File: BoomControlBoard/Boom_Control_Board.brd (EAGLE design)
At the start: 82.5 x 50.8 mm, 43 parts, among them J1 Servo Header, J2 FTDI Header, J7 455-1750-1-ND, U1 ATMEGA328P_TQFP, U2 3.3V/150mA, Y1 16MHz

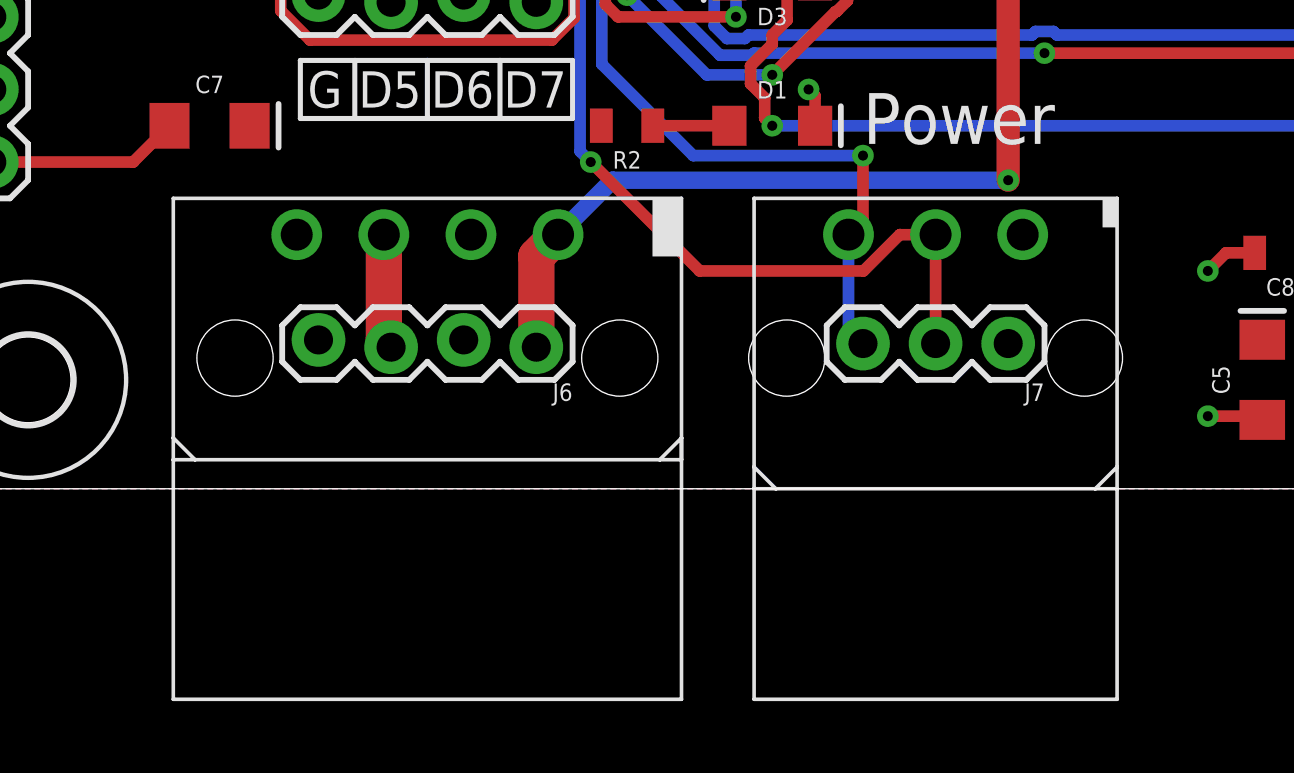
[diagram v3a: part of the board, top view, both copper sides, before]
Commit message: Improved Molex connector footprints.
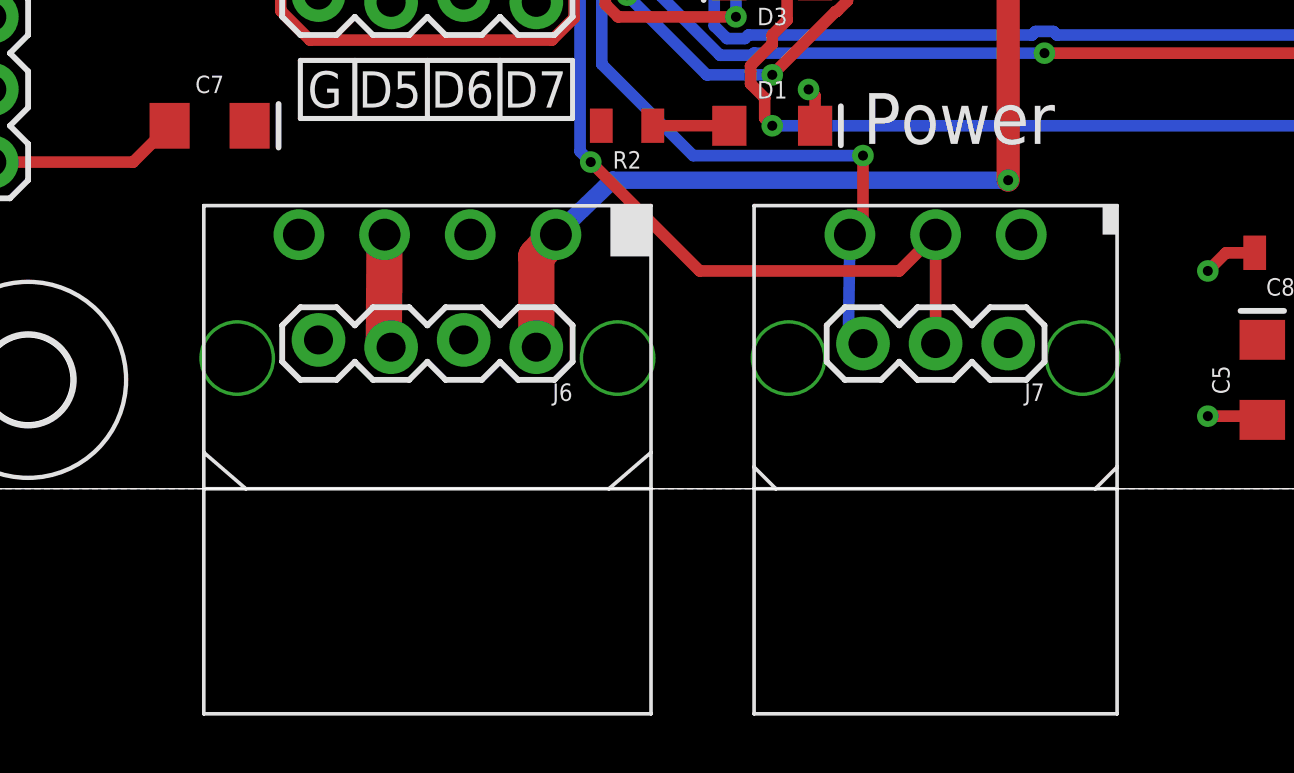
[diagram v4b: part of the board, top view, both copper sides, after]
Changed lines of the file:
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@@
 <attribute name="VALUE" x="24.765" y="13.589" size="0.6096" layer="27" font="vector" ratio="20" rot="R180" align="top-center"/>
 </element>
-<element name="H1" library="holes" library_urn="urn:adsk.eagle:library:237" package="3,0" package3d_urn="urn:adsk.eagle:package:14277/1" value="MOUNT-HOLE3.0" x="3.81" y="3.81" smashed="yes"/>
-<element name="H2" library="holes" library_urn="urn:adsk.eagle:library:237" package="3,0" package3d_urn="urn:adsk.eagle:package:14277/1" value="MOUNT-HOLE3.0" x="78.74" y="3.81" smashed="yes"/>
-<element name="H3" library="holes" library_urn="urn:adsk.eagle:library:237" package="3,0" package3d_urn="urn:adsk.eagle:package:14277/1" value="MOUNT-HOLE3.0" x="3.81" y="46.99" smashed="yes"/>
-<element name="H4" library="holes" library_urn="urn:adsk.eagle:library:237" package="3,0" package3d_urn="urn:adsk.eagle:package:14277/1" value="MOUNT-HOLE3.0" x="78.74" y="46.99" smashed="yes"/>
+<element name="H1" library="holes" library_urn="urn:adsk.eagle:library:237" package="3,0" package3d_urn="urn:adsk.eagle:package:14277/1" value="MOUNT-HOLE3.0" x="3.81" y="3.81" smashed="yes">
+<attribute name="POPULARITY" value="3" x="3.81" y="3.81" size="1.778" layer="27" display="off"/>
+</element>
+<element name="H2" library="holes" library_urn="urn:adsk.eagle:library:237" package="3,0" package3d_urn="urn:adsk.eagle:package:14277/1" value="MOUNT-HOLE3.0" x="78.74" y="3.81" smashed="yes">
+<attribute name="POPULARITY" value="3" x="78.74" y="3.81" size="1.778" layer="27" display="off"/>
+</element>
+<element name="H3" library="holes" library_urn="urn:adsk.eagle:library:237" package="3,0" package3d_urn="urn:adsk.eagle:package:14277/1" value="MOUNT-HOLE3.0" x="3.81" y="46.99" smashed="yes">
+<attribute name="POPULARITY" value="3" x="3.81" y="46.99" size="1.778" layer="27" display="off"/>
+</element>
+<element name="H4" library="holes" library_urn="urn:adsk.eagle:library:237" package="3,0" package3d_urn="urn:adsk.eagle:package:14277/1" value="MOUNT-HOLE3.0" x="78.74" y="46.99" smashed="yes">
+<attribute name="POPULARITY" value="3" x="78.74" y="46.99" size="1.778" layer="27" display="off"/>
+</element>
 <element name="S1" library="SparkFun-Switches" package="TACTILE_SWITCH_SMD_5.2MM" value="RESET" x="28.575" y="34.925" smashed="yes">
 <attribute name="NAME" x="28.575" y="37.592" size="0.6096" layer="25" font="vector" ratio="20" align="bottom-center"/>
@@
 <signal name="12V">
 <contactref element="U$1" pad="PIN1"/>
-<wire x1="24.257" y1="10.795" x2="22.352" y2="8.89" width="0.6096" layer="16"/>
+<wire x1="24.257" y1="10.795" x2="22.2758" y2="8.89" width="0.6096" layer="16"/>
 <wire x1="38.1" y1="10.795" x2="24.257" y2="10.795" width="0.6096" layer="16"/>
 <contactref element="U$4" pad="6"/>
@@
 <wire x1="39.0624" y1="30.47078125" x2="39.0624" y2="26.90635625" width="0.8128" layer="1"/>
 <contactref element="J6" pad="1"/>
-<wire x1="22.352" y1="8.89" x2="21.59" y2="8.128" width="1.27" layer="1"/>
+<wire x1="22.2758" y1="8.89" x2="21.59" y2="8.128" width="1.27" layer="1"/>
 <wire x1="21.59" y1="8.128" x2="21.59" y2="4.953" width="1.27" layer="1"/>
 </signal>
@@
 <contactref element="U$1" pad="PIN3"/>
 <contactref element="J6" pad="3"/>
-<wire x1="16.256" y1="8.89" x2="16.256" y2="5.207" width="1.27" layer="1"/>
+<wire x1="16.2814" y1="8.89" x2="16.256" y2="5.207" width="1.27" layer="1"/>
 <wire x1="16.256" y1="5.207" x2="16.51" y2="4.953" width="1.27" layer="1"/>
 </signal>
@@
 <via x="33.02" y="11.6558" extent="1-16" drill="0.35"/>
 <wire x1="33.02" y1="11.6558" x2="33.02" y2="9.398" width="0.4064" layer="1"/>
-<wire x1="33.02" y1="9.398" x2="32.512" y2="8.89" width="0.4064" layer="1"/>
+<wire x1="33.02" y1="9.398" x2="32.5628" y2="8.89" width="0.4064" layer="1"/>
 <wire x1="23.8816" y1="23.495" x2="23.8816" y2="14.8534" width="0.4064" layer="16"/>
 <wire x1="23.8816" y1="14.8534" x2="27.0792" y2="11.6558" width="0.4064" layer="16"/>
 <wire x1="27.0792" y1="11.6558" x2="33.02" y2="11.6558" width="0.4064" layer="16"/>
 <contactref element="J7" pad="3"/>
-<wire x1="32.512" y1="8.89" x2="32.512" y2="5.588" width="0.4064" layer="16"/>
+<wire x1="32.5628" y1="8.89" x2="32.512" y2="5.588" width="0.4064" layer="16"/>
 <wire x1="32.512" y1="5.588" x2="33.02" y2="5.08" width="0.4064" layer="16"/>
 </signal>
@@
 <wire x1="23.1224" y1="23.180525" x2="23.26" y2="23.042925" width="0.4064" layer="1"/>
 <wire x1="23.26" y1="23.042925" x2="23.26" y2="21.9388375" width="0.4064" layer="1"/>
-<wire x1="34.30805625" y1="8.89" x2="35.56" y2="8.89" width="0.4064" layer="1"/>
-<wire x1="33.03805625" y1="7.62" x2="34.30805625" y2="8.89" width="0.4064" layer="1"/>
-<wire x1="27.305" y1="7.62" x2="33.03805625" y2="7.62" width="0.4064" layer="1"/>
 <wire x1="23.1224" y1="11.8026" x2="23.495" y2="11.43" width="0.4064" layer="16"/>
 <via x="23.495" y="11.43" extent="1-16" drill="0.35"/>
@@
 <contactref element="J7" pad="2"/>
 <wire x1="35.56" y1="8.89" x2="35.56" y2="5.08" width="0.4064" layer="1"/>
+<wire x1="34.29" y1="7.62" x2="35.56" y2="8.89" width="0.4064" layer="1"/>
+<wire x1="27.305" y1="7.62" x2="34.29" y2="7.62" width="0.4064" layer="1"/>
 </signal>
 <signal name="PB2">
@@
 <mfgpreviewcolor name="substratecolor" color="0xFF786E46"/>
 </mfgpreviewcolors>
-<errors>
-</errors>
 </board>
 </drawing>

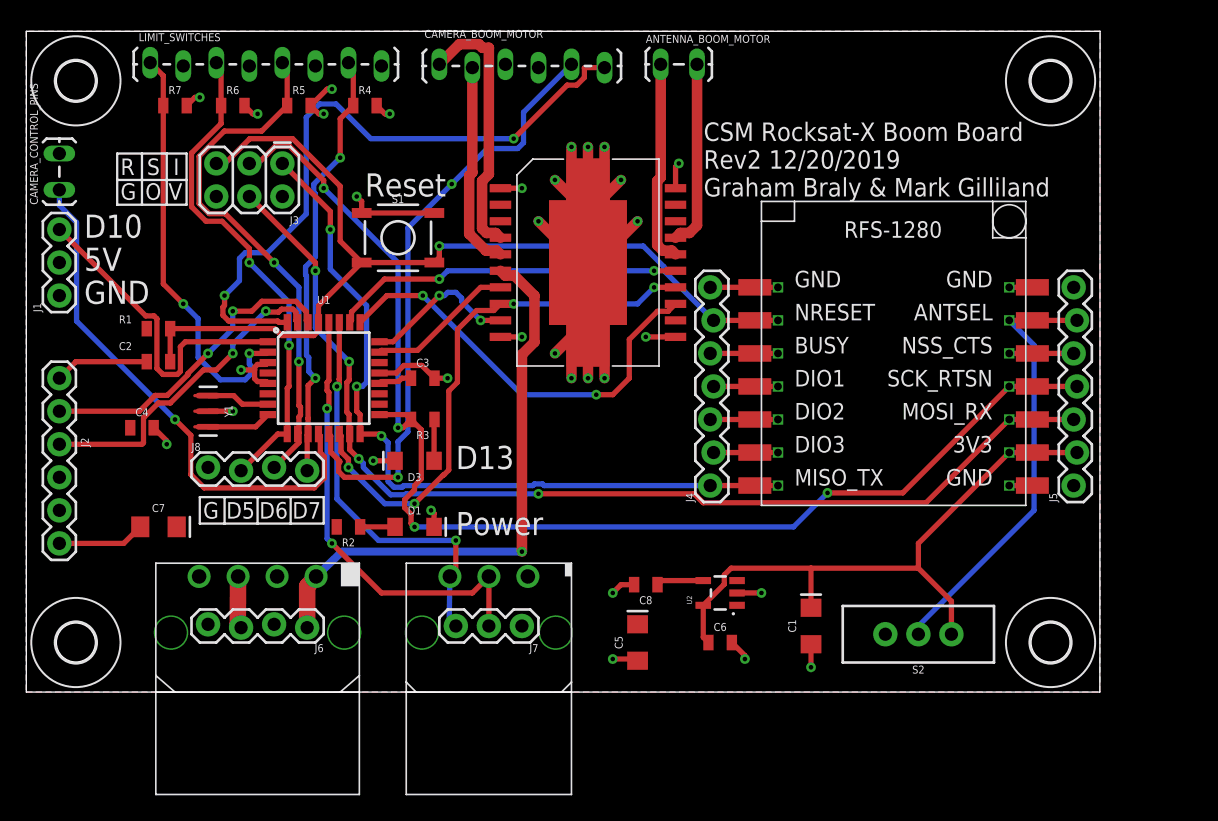
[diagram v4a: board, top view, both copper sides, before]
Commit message: Lots of Labels added, GND connections added, component labels embiggened, traces rerouted.
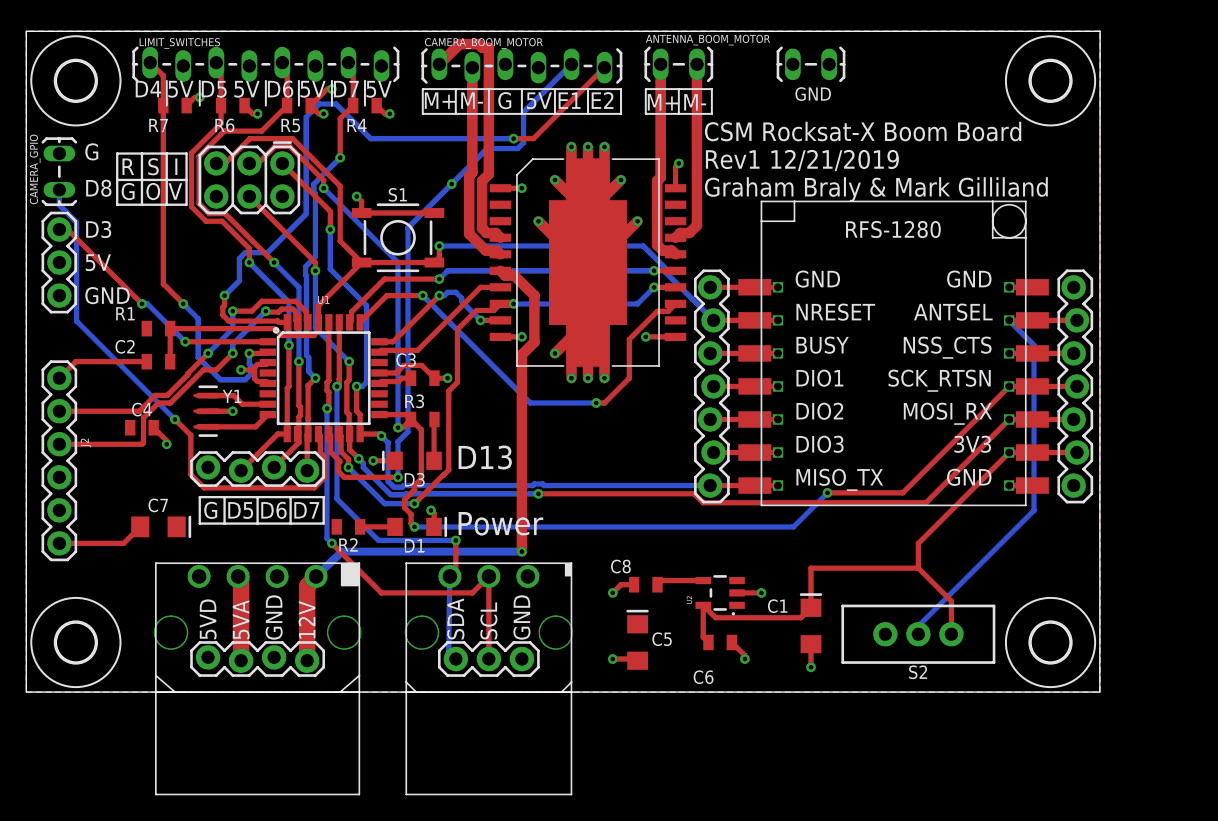
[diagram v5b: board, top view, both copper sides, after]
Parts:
- added GND: (no value), SparkFun-Connectors:1X02_LOCK_LONGPADS
- D1, D3: value GREEN -> (none)
- J1: value Servo Header -> Servo
- J2: value FTDI Header -> FTDI
- J7: value 455-1750-1-ND -> (none)
- S2: value (none) -> ANTENNA_SELECT
- U1: value ATMEGA328P_TQFP -> ATMEGA328P
- moved J6 2.54 mm to (21.6, 2.54)
- moved J7 2.54 mm to (38.1, 2.54)
- renumbered CAMERA_CONTROL_PINS to CAMERA_GPIO
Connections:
- net GND: now also GND.1, GND.2
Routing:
- net PD3: track 25.0 -> 19.6 mm, vias 0 -> 2
- net SDA: track 31.1 -> 33.6 mm
- net 12V: track 44.3 -> 46.8 mm
- net SCL: track 35.3 -> 37.8 mm
- net 5V_ACT: track 4.04 -> 6.57 mm
- net 3V3: track 47.3 -> 46.4 mm
- net PC2: track 32.9 -> 33.4 mm
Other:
- board text added: "12V"
- board text added: "5VA"
- board text added: "5VD"
- board text added: "CSM Rocksat-X Boom Board Rev1 12/21/2019 Graham Braly & Mark Gilliland"
- board text added: "D3"
- board text added: "D4"
- board text added: "D8"
- board text added: "E1"
- board text added: "E2"
- board text added: "M+"
- board text added: "M-"
- board text added: "SCL"
- board text added: "SDA"
- board text removed: "CSM Rocksat-X Boom Board Rev2 12/20/2019 Graham Braly & Mark Gilliland"
- board text removed: "D10"
- board text removed: "Reset"
